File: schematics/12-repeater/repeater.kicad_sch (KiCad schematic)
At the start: 13 parts, among them J1 Cat5, J2 Mini-DIN, U1 PCA9600D

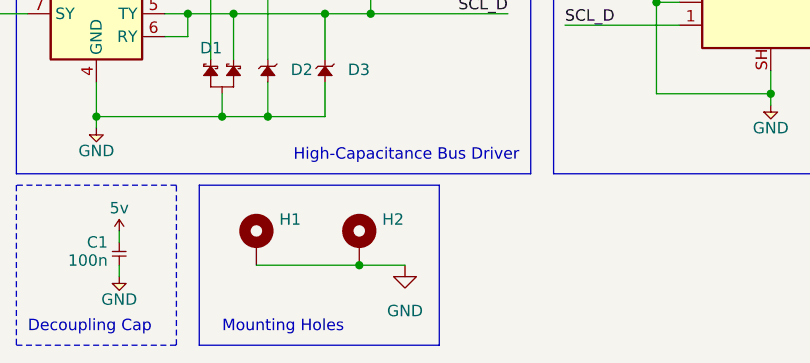
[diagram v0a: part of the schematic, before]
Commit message: Fix minor symbol errors
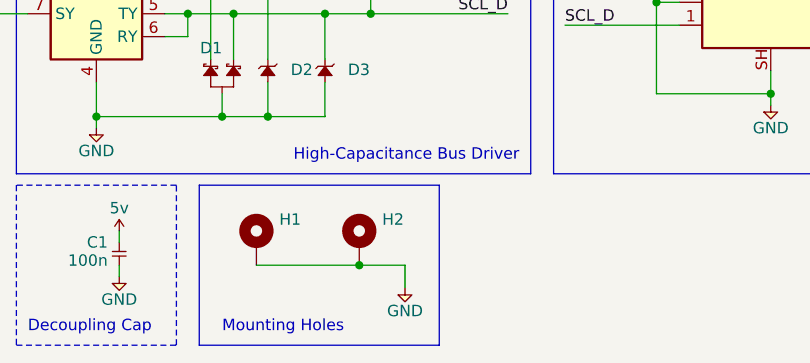
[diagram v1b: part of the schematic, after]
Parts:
- H1, H2: footprint royale:MountingHole_Pad -> royale:MountingHole_3.2mm_M3_Pad_Via
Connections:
- net 1v8 renamed 5v

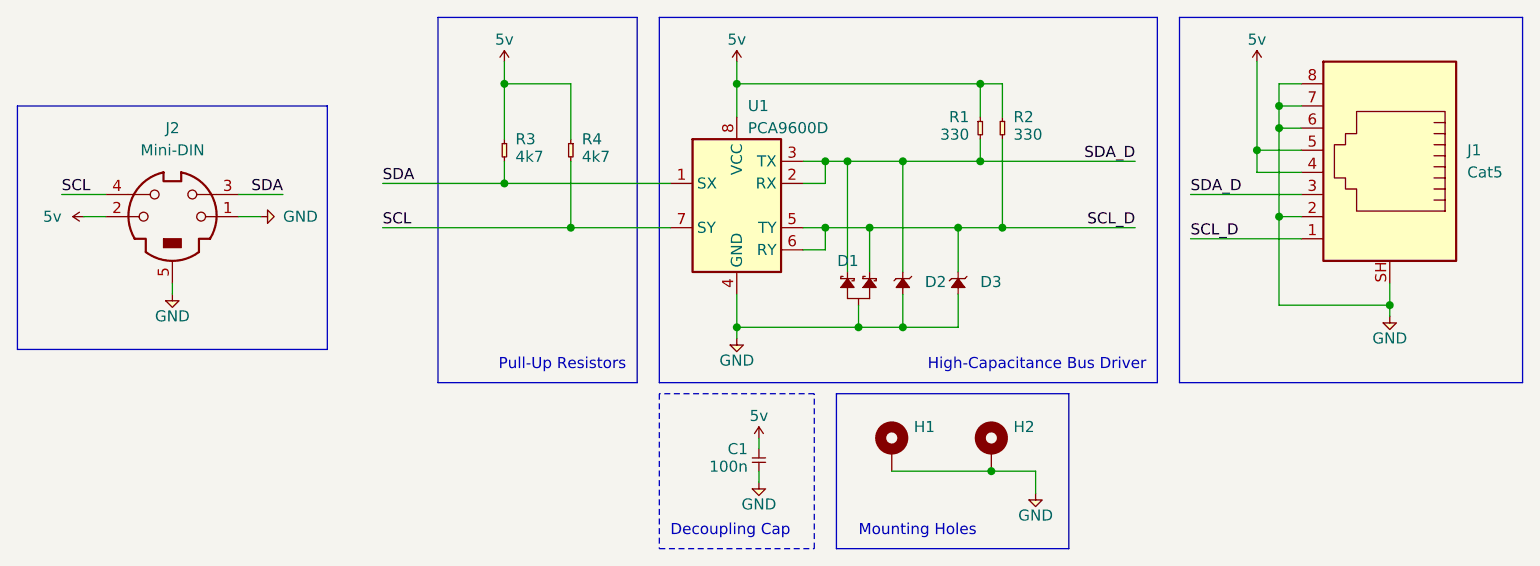
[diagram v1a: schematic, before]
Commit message: Reorder RJ45 pins to simplify board layout
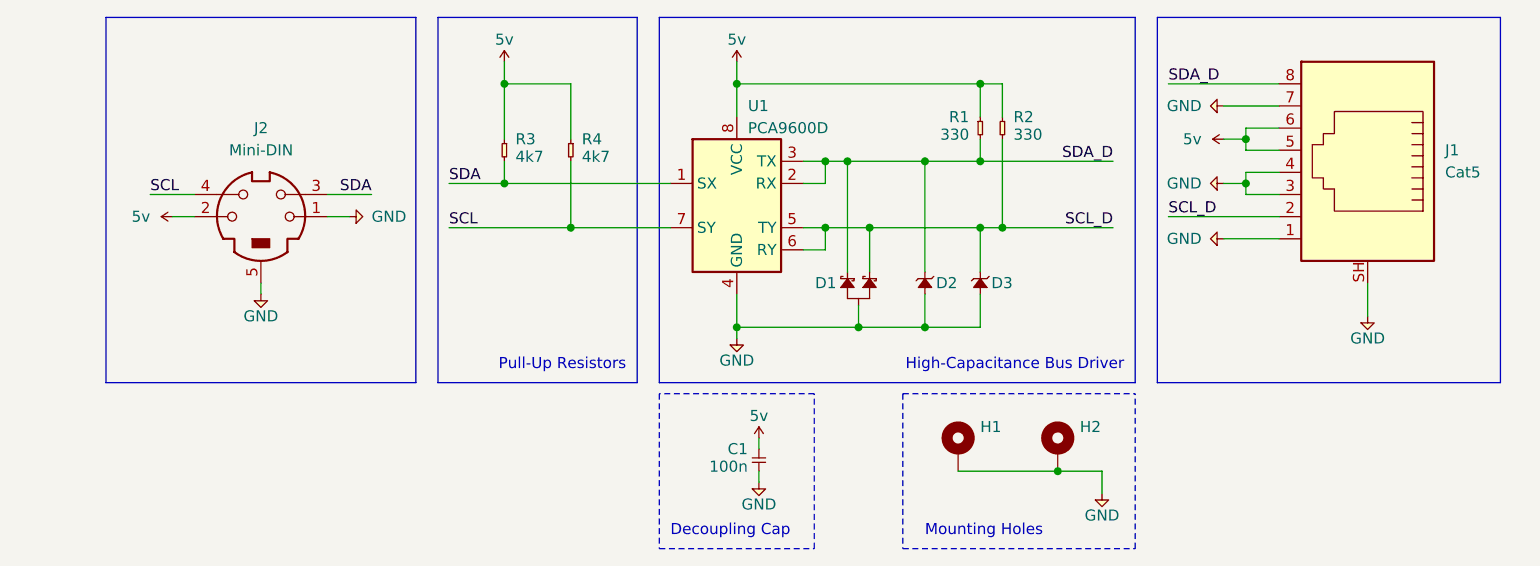
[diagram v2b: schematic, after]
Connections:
- net 5v: now also J1.6; no longer J1.4
- net GND: now also J1.1, J1.3, J1.4; no longer J1.2, J1.6, J1.8
- net SCL_D: now also J1.2; no longer J1.1
- net SDA_D: now also J1.8; no longer J1.3
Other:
- moved on the sheet: D2, D3, H1, H2, J1, J2
